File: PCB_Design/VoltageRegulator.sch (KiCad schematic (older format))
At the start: 7 parts

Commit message: Programación por UART-Botones
Se añadieron los botones con el circuito de debouncing, un botón de enable para la esp32 y los pines para la programacion.
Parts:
- IC: symbol MIC37303YME-TR:MIC37303YME -> PCB_Design-rescue:MIC37303YME-MIC37303YME-TR
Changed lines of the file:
@@
 $Descr User 6000 6000
 encoding utf-8
-Sheet 3 3
+Sheet 3 7
 Title "Circuito para regular la tensión "
 Date ""
@@
 $EndDescr
 $Comp
-L power:GND #PWR?
+L power:GND #PWR0108
 U 1 1 61A03FAF
 P 3425 3225
-F 0 "#PWR?" H 3425 2975 50  0001 C CNN
+F 0 "#PWR0108" H 3425 2975 50  0001 C CNN
 F 1 "GND" H 3430 3052 50  0000 C CNN
 F 2 "" H 3425 3225 50  0001 C CNN
@@
 	2475 2175 2475 2625
 $Comp
-L power:GND #PWR?
+L power:GND #PWR0109
 U 1 1 61A104AE
 P 1525 3225
-F 0 "#PWR?" H 1525 2975 50  0001 C CNN
+F 0 "#PWR0109" H 1525 2975 50  0001 C CNN
 F 1 "GND" H 1530 3052 50  0000 C CNN
 F 2 "" H 1525 3225 50  0001 C CNN
@@
 $EndComp
 $Comp
-L MIC37303YME-TR:MIC37303YME IC
+L PCB_Design-rescue:MIC37303YME-MIC37303YME-TR IC
 U 1 1 61A02BF7
 P 2525 2075
+AR Path="/61A02BF7" Ref="IC"  Part="1"
+AR Path="/619FB45F/61A02BF7" Ref="IC"  Part="1"
 F 0 "IC" H 3225 2340 50  0000 C CNN
 F 1 "MIC37303YME" H 3225 2249 50  0000 C CNN
@@
 $EndComp
 $Comp
-L power:GND #PWR?
+L power:GND #PWR0110
 U 1 1 61A038ED
 P 3025 3225
-F 0 "#PWR?" H 3025 2975 50  0001 C CNN
+F 0 "#PWR0110" H 3025 2975 50  0001 C CNN
 F 1 "GND" H 3030 3052 50  0000 C CNN
 F 2 "" H 3025 3225 50  0001 C CNN
@@
 Connection ~ 4050 2075
 $Comp
-L power:GND #PWR?
+L power:GND #PWR0111
 U 1 1 61A59489
 P 4050 3225
-F 0 "#PWR?" H 4050 2975 50  0001 C CNN
+F 0 "#PWR0111" H 4050 2975 50  0001 C CNN
 F 1 "GND" H 4055 3052 50  0000 C CNN
 F 2 "" H 4050 3225 50  0001 C CNN
@@
 $EndComp
 $Comp
-L power:GND #PWR?
+L power:GND #PWR0112
 U 1 1 61A59B9D
 P 4525 3225
-F 0 "#PWR?" H 4525 2975 50  0001 C CNN
+F 0 "#PWR0112" H 4525 2975 50  0001 C CNN
 F 1 "GND" H 4530 3052 50  0000 C CNN
 F 2 "" H 4525 3225 50  0001 C CNN

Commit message: Partialy finished schematic
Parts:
- added SW_ONOFF: SW_Push, symbol Switch:SW_Push
- renumbered FlagLED to FlagLED_R
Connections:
- net Batt: now also SW_ONOFF.1; no longer FlagLED_R.2 (A), IC.2 (EN), IC.3 (VIN_1), IC.4 (VIN_2), Steve.1
- new net: FlagLED_R.2 (A), IC.2 (EN), IC.3 (VIN_1), IC.4 (VIN_2), SW_ONOFF.2, Steve.1
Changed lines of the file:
@@
 	1    0    0    -1
 $EndComp
-Text HLabel 1125 2075 0    50   Input ~ 0
+Text HLabel 850  2075 0    50   Input ~ 0
 Batt
 $Comp
@@
 $EndComp
 $Comp
-L Device:LED FlagLED
+L Device:LED FlagLED_R
 U 1 1 61A2093A
 P 2025 2275
-F 0 "FlagLED" H 2175 2375 50  0000 R CNN
+F 0 "FlagLED_R" H 2175 2375 50  0000 R CNN
 F 1 "LED" V 1973 2157 50  0001 R CNN
 F 2 "" H 2025 2275 50  0001 C CNN
@@
 	2025 2825 2525 2825
 Wire Wire Line
-	1125 2075 1525 2075
+	850  2075 950  2075
 Wire Wire Line
 	1525 2075 1525 2475
@@
 Text HLabel 4925 2075 2    50   Output ~ 0
 3.34V
+$Comp
+L Switch:SW_Push SW_ONOFF
+U 1 1 61C32C50
+P 1150 2075
+F 0 "SW_ONOFF" H 1150 2360 50  0000 C CNN
+F 1 "SW_Push" H 1150 2269 50  0000 C CNN
+F 2 "" H 1150 2275 50  0001 C CNN
+F 3 "~" H 1150 2275 50  0001 C CNN
+	1    1150 2075
+	1    0    0    -1
+$EndComp
+Wire Wire Line
+	1350 2075 1525 2075
 $EndSCHEMATC

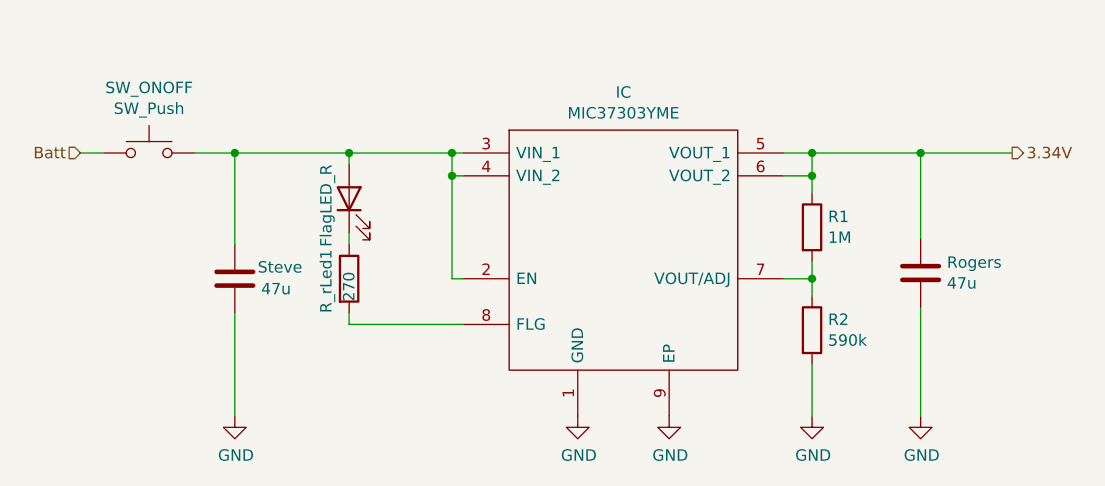
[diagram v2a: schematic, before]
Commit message: huellas agregadas
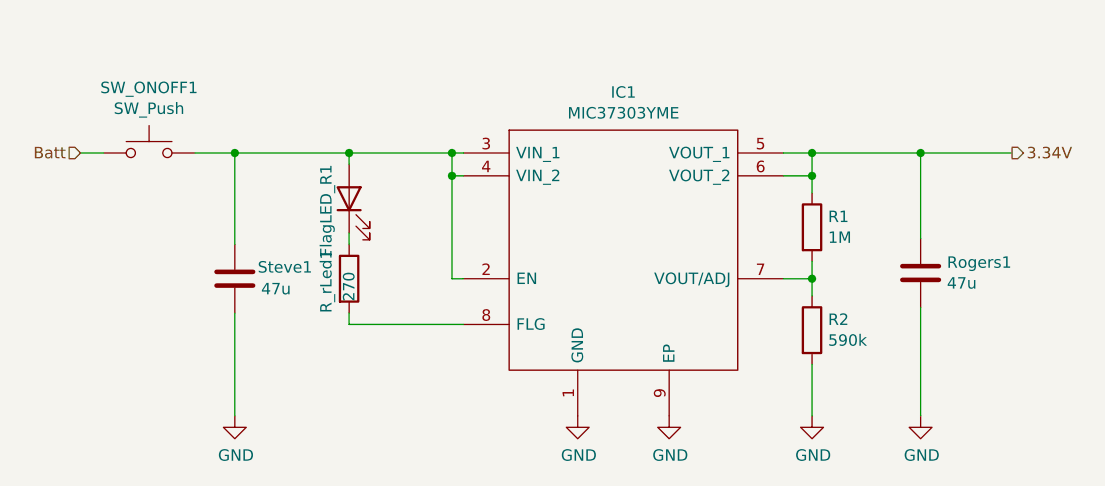
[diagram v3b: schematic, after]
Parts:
- FlagLED_R1: renamed from FlagLED_R; footprint (none) -> LED_SMD:LED_0805_2012Metric_Pad1.15x1.40mm_HandSolder
- IC: footprint SOIC127P602X168-9N -> Package_SO:SOIC-8-1EP_3.9x4.9mm_P1.27mm_EP2.514x3.2mm
- R1, R2, R_rLed1: footprint (none) -> Resistor_SMD:R_0805_2012Metric_Pad1.20x1.40mm_HandSolder
- Rogers1: renamed from Rogers; footprint (none) -> Capacitor_SMD:CP_Elec_6.3x5.9
- SW_ONOFF1: renamed from SW_ONOFF; footprint (none) -> Connector_TE-Connectivity:TE_MATE-N-LOK_1-770866-x_1x02_P4.14mm_Vertical
- Steve1: renamed from Steve; footprint (none) -> Capacitor_SMD:CP_Elec_6.3x5.9
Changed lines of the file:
@@
 Batt
 $Comp
-L Device:C Steve
+L Device:C Steve1
 U 1 1 61A07986
 P 1525 2625
-F 0 "Steve" H 1625 2675 50  0000 L CNN
+F 0 "Steve1" H 1625 2675 50  0000 L CNN
 F 1 "47u" H 1640 2580 50  0000 L CNN
-F 2 "" H 1563 2475 50  0001 C CNN
+F 2 "Capacitor_SMD:CP_Elec_6.3x5.9" H 1563 2475 50  0001 C CNN
 F 3 "~" H 1525 2625 50  0001 C CNN
 	1    1525 2625
@@
 F 0 "R_rLed1" V 1925 2475 50  0000 L CNN
 F 1 "270" V 2025 2525 50  0000 L CNN
-F 2 "" V 1955 2625 50  0001 C CNN
+F 2 "Resistor_SMD:R_0805_2012Metric_Pad1.20x1.40mm_HandSolder" V 1955 2625 50  0001 C CNN
 F 3 "~" H 2025 2625 50  0001 C CNN
 	1    2025 2625
@@
 $EndComp
 $Comp
-L Device:LED FlagLED_R
+L Device:LED FlagLED_R1
 U 1 1 61A2093A
 P 2025 2275
-F 0 "FlagLED_R" H 2175 2375 50  0000 R CNN
+F 0 "FlagLED_R1" H 2175 2375 50  0000 R CNN
 F 1 "LED" V 1973 2157 50  0001 R CNN
-F 2 "" H 2025 2275 50  0001 C CNN
+F 2 "LED_SMD:LED_0805_2012Metric_Pad1.15x1.40mm_HandSolder" H 2025 2275 50  0001 C CNN
 F 3 "~" H 2025 2275 50  0001 C CNN
 	1    2025 2275
@@
 P 2525 2075
 AR Path="/61A02BF7" Ref="IC"  Part="1"
-AR Path="/619FB45F/61A02BF7" Ref="IC"  Part="1"
-F 0 "IC" H 3225 2340 50  0000 C CNN
+AR Path="/619FB45F/61A02BF7" Ref="IC1"  Part="1"
+F 0 "IC1" H 3225 2340 50  0000 C CNN
 F 1 "MIC37303YME" H 3225 2249 50  0000 C CNN
-F 2 "SOIC127P602X168-9N" H 3175 3225 50  0001 L CNN
+F 2 "Package_SO:SOIC-8-1EP_3.9x4.9mm_P1.27mm_EP2.514x3.2mm" H 3175 3225 50  0001 L CNN
 F 3 "http://www.microchip.com/mymicrochip/filehandler.aspx?ddocname=en581526" H 3175 3125 50  0001 L CNN
 F 4 "LDO Voltage Regulators 3A, Low Voltage uCap LDO Regulator" H 3175 3025 50  0001 L CNN "Description"
@@
 F 0 "R1" H 4120 2446 50  0000 L CNN
 F 1 "1M" H 4120 2355 50  0000 L CNN
-F 2 "" V 3980 2400 50  0001 C CNN
+F 2 "Resistor_SMD:R_0805_2012Metric_Pad1.20x1.40mm_HandSolder" V 3980 2400 50  0001 C CNN
 F 3 "~" H 4050 2400 50  0001 C CNN
 	1    4050 2400
@@
 F 0 "R2" H 4120 2896 50  0000 L CNN
 F 1 "590k" H 4120 2805 50  0000 L CNN
-F 2 "" V 3980 2850 50  0001 C CNN
+F 2 "Resistor_SMD:R_0805_2012Metric_Pad1.20x1.40mm_HandSolder" V 3980 2850 50  0001 C CNN
 F 3 "~" H 4050 2850 50  0001 C CNN
 	1    4050 2850
@@
 	4050 2175 4050 2250
 $Comp
-L Device:C Rogers
+L Device:C Rogers1
 U 1 1 61A5751A
 P 4525 2600
-F 0 "Rogers" H 4640 2646 50  0000 L CNN
+F 0 "Rogers1" H 4640 2646 50  0000 L CNN
 F 1 "47u" H 4640 2555 50  0000 L CNN
-F 2 "" H 4563 2450 50  0001 C CNN
+F 2 "Capacitor_SMD:CP_Elec_6.3x5.9" H 4563 2450 50  0001 C CNN
 F 3 "~" H 4525 2600 50  0001 C CNN
 	1    4525 2600
@@
 Text HLabel 4925 2075 2    50   Output ~ 0
 3.34V
-$Comp
-L Switch:SW_Push SW_ONOFF
+Wire Wire Line
+	1350 2075 1525 2075
+$Comp
+L Switch:SW_Push SW_ONOFF1
 U 1 1 61C32C50
 P 1150 2075
-F 0 "SW_ONOFF" H 1150 2360 50  0000 C CNN
+F 0 "SW_ONOFF1" H 1150 2360 50  0000 C CNN
 F 1 "SW_Push" H 1150 2269 50  0000 C CNN
-F 2 "" H 1150 2275 50  0001 C CNN
+F 2 "Connector_TE-Connectivity:TE_MATE-N-LOK_1-770866-x_1x02_P4.14mm_Vertical" H 1150 2275 50  0001 C CNN
 F 3 "~" H 1150 2275 50  0001 C CNN
 	1    1150 2075
 	1    0    0    -1
 $EndComp
-Wire Wire Line
-	1350 2075 1525 2075
 $EndSCHEMATC

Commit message: PCB terminada
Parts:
- R1: value 1M -> 6.98k; footprint Resistor_SMD:R_0805_2012Metric_Pad1.20x1.40mm_HandSolder -> Resistor_SMD:R_1206_3216Metric_Pad1.30x1.75mm_HandSolder
- R2: value 590k -> 4.02k; footprint Resistor_SMD:R_0805_2012Metric_Pad1.20x1.40mm_HandSolder -> Resistor_SMD:R_1206_3216Metric_Pad1.30x1.75mm_HandSolder
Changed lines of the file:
@@
 P 4050 2400
 F 0 "R1" H 4120 2446 50  0000 L CNN
-F 1 "1M" H 4120 2355 50  0000 L CNN
-F 2 "Resistor_SMD:R_0805_2012Metric_Pad1.20x1.40mm_HandSolder" V 3980 2400 50  0001 C CNN
+F 1 "6.98k" H 4120 2355 50  0000 L CNN
+F 2 "Resistor_SMD:R_1206_3216Metric_Pad1.30x1.75mm_HandSolder" V 3980 2400 50  0001 C CNN
 F 3 "~" H 4050 2400 50  0001 C CNN
 	1    4050 2400
@@
 P 4050 2850
 F 0 "R2" H 4120 2896 50  0000 L CNN
-F 1 "590k" H 4120 2805 50  0000 L CNN
-F 2 "Resistor_SMD:R_0805_2012Metric_Pad1.20x1.40mm_HandSolder" V 3980 2850 50  0001 C CNN
+F 1 "4.02k" H 4120 2805 50  0000 L CNN
+F 2 "Resistor_SMD:R_1206_3216Metric_Pad1.30x1.75mm_HandSolder" V 3980 2850 50  0001 C CNN
 F 3 "~" H 4050 2850 50  0001 C CNN
 	1    4050 2850
